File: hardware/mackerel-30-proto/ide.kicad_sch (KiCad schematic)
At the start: 0 parts

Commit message: Mostly fixed the SIMM-72 footprint
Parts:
- added C29, C30: C, Capacitor_THT:C_Disc_D4.3mm_W1.9mm_P5.00mm, symbol Device:C
- added C31: 1000uF, Capacitor_THT:CP_Radial_D10.0mm_P5.00mm, symbol Device:C_Polarized
- added C32: 470uF, Capacitor_THT:CP_Radial_D8.0mm_P3.50mm, symbol Device:C_Polarized_US
- added D4: LED, LED_THT:LED_D5.0mm, symbol Device:LED
- added J12: Screw_Terminal_01x04, TerminalBlock:TerminalBlock_bornier-4_P5.08mm, symbol Connector:Screw_Terminal_01x04
- added J13: Conn_02x20_Odd_Even, Connector_IDC:IDC-Header_2x20_P2.54mm_Vertical, symbol Connector_Generic:Conn_02x20_Odd_Even
- added R26, R27: 4k7, Resistor_THT:R_Axial_DIN0207_L6.3mm_D2.5mm_P7.62mm_Horizontal, symbol Device:R
- added R28: 470, Resistor_THT:R_Axial_DIN0207_L6.3mm_D2.5mm_P7.62mm_Horizontal, symbol Device:R
- added U12, U13: 74HC245, Package_DIP:DIP-20_W7.62mm_Socket, symbol 74xx:74HC245
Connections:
- new net: D4.2 (A), R28.2
- new net: D4.1 (K), J13.39 (Pin_39)
- new net +12V: C31.1, J12.1 (Pin_1)
- new net +5V: C29.1, C30.1, C32.1, J12.4 (Pin_4), R28.1, U12.20 (VCC), U13.20 (VCC)
- new net A1: J13.35 (Pin_35)
- new net A2: J13.33 (Pin_33)
- new net A3: J13.36 (Pin_36)
- new net D16: U13.18 (B0)
- new net D17: U13.17 (B1)
- new net D18: U13.16 (B2)
- new net D19: U13.15 (B3)
- new net D20: U13.14 (B4)
- new net D21: U13.13 (B5)
- new net D22: U13.12 (B6)
- new net D23: U13.11 (B7)
- new net D24: U12.18 (B0)
- new net D25: U12.17 (B1)
- new net D26: U12.16 (B2)
- new net D27: U12.15 (B3)
- new net D28: U12.14 (B4)
- new net D29: U12.13 (B5)
- new net D30: U12.12 (B6)
- new net D31: U12.11 (B7)
- new net GND: C29.2, C30.2, C31.2, C32.2, J12.2 (Pin_2), J12.3 (Pin_3), J13.19 (Pin_19), J13.2 (Pin_2), J13.22 (Pin_22), J13.24 (Pin_24), J13.26 (Pin_26), J13.30 (Pin_30), J13.40 (Pin_40), R26.1, R27.1, U12.10 (GND), U13.10 (GND)
- new net IDE_D0: J13.17 (Pin_17), U12.2 (A0)
- new net IDE_D1: J13.15 (Pin_15), U12.3 (A1)
- new net IDE_D10: J13.8 (Pin_8), U13.7 (A5)
- new net IDE_D11: J13.10 (Pin_10), U13.6 (A4)
- new net IDE_D12: J13.12 (Pin_12), U13.5 (A3)
- new net IDE_D13: J13.14 (Pin_14), U13.4 (A2)
- new net IDE_D14: J13.16 (Pin_16), U13.3 (A1)
- new net IDE_D15: J13.18 (Pin_18), U13.2 (A0)
- new net IDE_D2: J13.13 (Pin_13), U12.4 (A2)
- new net IDE_D3: J13.11 (Pin_11), U12.5 (A3)
- new net IDE_D4: J13.9 (Pin_9), U12.6 (A4)
- new net IDE_D5: J13.7 (Pin_7), U12.7 (A5)
- new net IDE_D6: J13.5 (Pin_5), U12.8 (A6)
- new net IDE_D7: J13.3 (Pin_3), U12.9 (A7)
- new net IDE_D8: J13.4 (Pin_4), U13.9 (A7)
- new net IDE_D9: J13.6 (Pin_6), U13.8 (A6)
- new net IDE_INT: J13.31 (Pin_31), R27.2
- new net IDE_RDY: J13.27 (Pin_27), R26.2
- new net R/W: U12.1 (A->B), U13.1 (A->B)
- new net /IDE_BUF: U12.19 (CE), U13.19 (CE)
- new net /IDE_CS0: J13.37 (Pin_37)
- new net /IDE_CS1: J13.38 (Pin_38)
- new net /IDE_RD: J13.25 (Pin_25)
- new net /IDE_WR: J13.23 (Pin_23)
- new net /RESET: J13.1 (Pin_1)
- no-connect marks 0 -> 6
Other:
- note added: "Activity LED"
- note added: "Basically DTACK, active HIGH"
- note added: "IDE Header"
- note added: "IRQ, active HIGH"
- note added: "NOTE: High and low bytes swapped between the CPU and the IDE header"

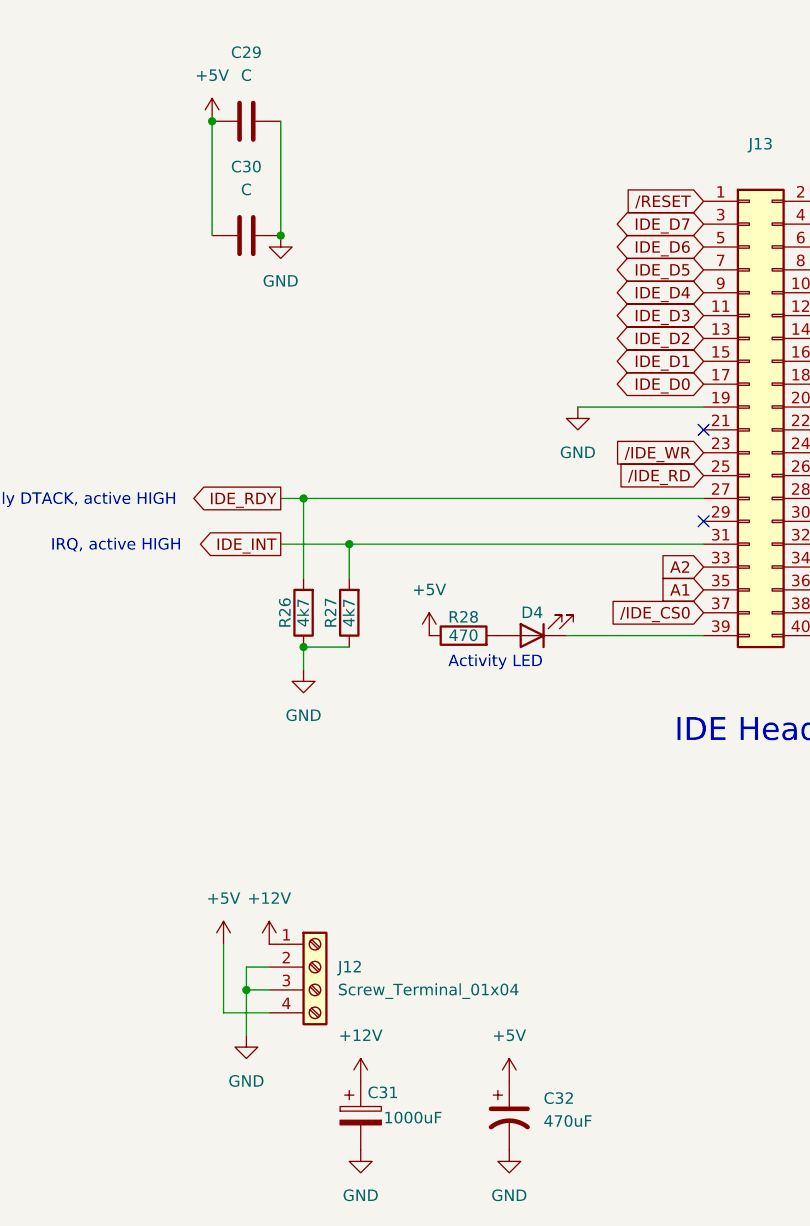
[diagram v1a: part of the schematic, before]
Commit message: Add DS1233 for reset
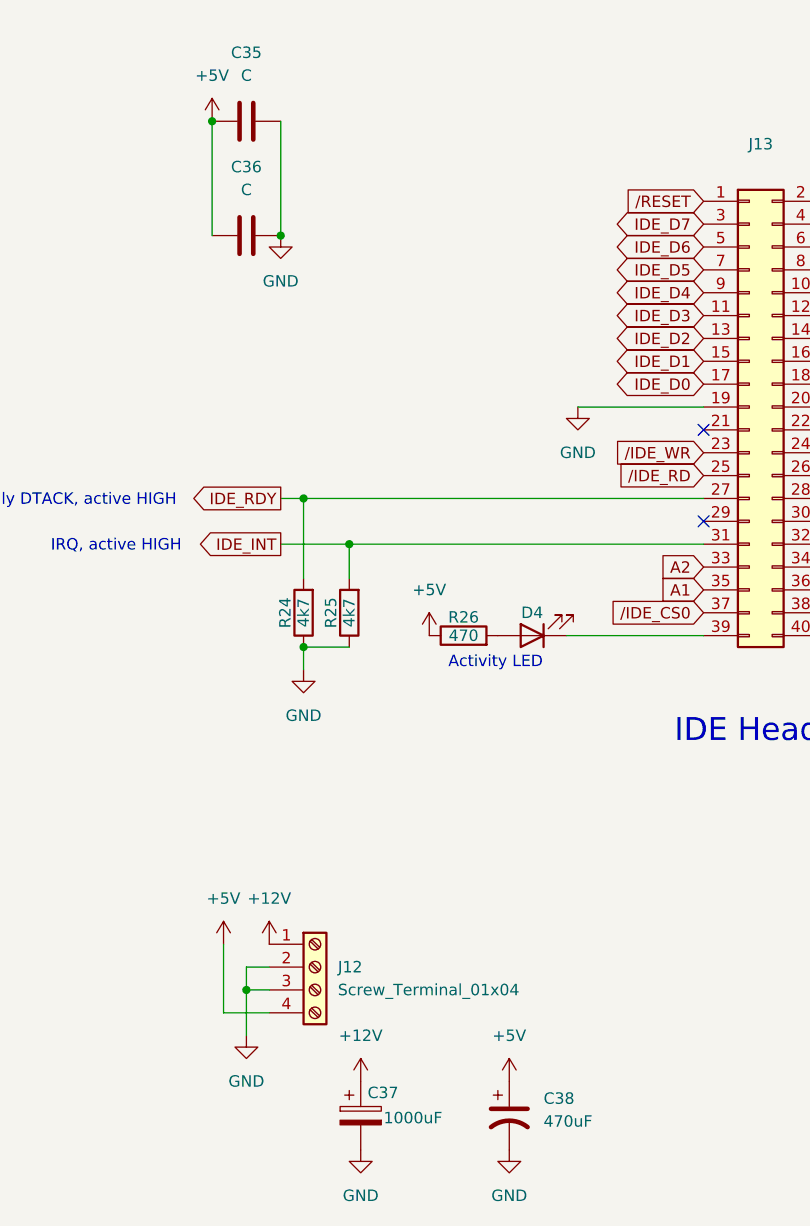
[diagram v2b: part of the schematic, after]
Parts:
- renumbered C29 to C35, C30 to C36, C31 to C37, C32 to C38, R26 to R24, R27 to R25, R28 to R26
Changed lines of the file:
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@@
 		(on_board yes)
 		(dnp no)
-		(property "Reference" "C31"
+		(property "Reference" "C37"
 			(at 159.512 148.59 0)
 			(effects
@@
 			(project "mackerel-30-proto"
 				(path "/9307474f-ec99-494d-b4c9-fbd0b10ce86a/b80ba0ac-a3c1-4262-b297-c092dfcb6fec"
-					(reference "C31")
+					(reference "C37")
 					(unit 1)
 				)
@@
 		(on_board yes)
 		(dnp no)
-		(property "Reference" "R28"
+		(property "Reference" "R26"
 			(at 170.18 95.758 90)
 			(effects
@@
 			(project "mackerel-30-proto"
 				(path "/9307474f-ec99-494d-b4c9-fbd0b10ce86a/b80ba0ac-a3c1-4262-b297-c092dfcb6fec"
-					(reference "R28")
+					(reference "R26")
 					(unit 1)
 				)
@@
 		(dnp no)
 		(fields_autoplaced yes)
-		(property "Reference" "C32"
+		(property "Reference" "C38"
 			(at 179.07 149.2249 0)
 			(effects
@@
 			(project "mackerel-30-proto"
 				(path "/9307474f-ec99-494d-b4c9-fbd0b10ce86a/b80ba0ac-a3c1-4262-b297-c092dfcb6fec"
-					(reference "C32")
+					(reference "C38")
 					(unit 1)
 				)
@@
 		(on_board yes)
 		(dnp no)
-		(property "Reference" "R26"
+		(property "Reference" "R24"
 			(at 150.368 95.25 90)
 			(effects
@@
 			(project "mackerel-30-proto"
 				(path "/9307474f-ec99-494d-b4c9-fbd0b10ce86a/b80ba0ac-a3c1-4262-b297-c092dfcb6fec"
-					(reference "R26")
+					(reference "R24")
 					(unit 1)
 				)
@@
 		(dnp no)
 		(fields_autoplaced yes)
-		(property "Reference" "C29"
+		(property "Reference" "C35"
 			(at 146.05 33.02 90)
 			(effects
@@
 			(project "mackerel-30-proto"
 				(path "/9307474f-ec99-494d-b4c9-fbd0b10ce86a/b80ba0ac-a3c1-4262-b297-c092dfcb6fec"
-					(reference "C29")
+					(reference "C35")
 					(unit 1)
 				)
@@
 		(dnp no)
 		(fields_autoplaced yes)
-		(property "Reference" "C30"
+		(property "Reference" "C36"
 			(at 146.05 45.72 90)
 			(effects
@@
 			(project "mackerel-30-proto"
 				(path "/9307474f-ec99-494d-b4c9-fbd0b10ce86a/b80ba0ac-a3c1-4262-b297-c092dfcb6fec"
-					(reference "C30")
+					(reference "C36")
 					(unit 1)
 				)
@@
 		(on_board yes)
 		(dnp no)
-		(property "Reference" "R27"
+		(property "Reference" "R25"
 			(at 155.448 95.25 90)
 			(effects
@@
 			(project "mackerel-30-proto"
 				(path "/9307474f-ec99-494d-b4c9-fbd0b10ce86a/b80ba0ac-a3c1-4262-b297-c092dfcb6fec"
-					(reference "R27")
-					(unit 1)
-				)
+					(reference "R25")
+					(unit 1)
+				)

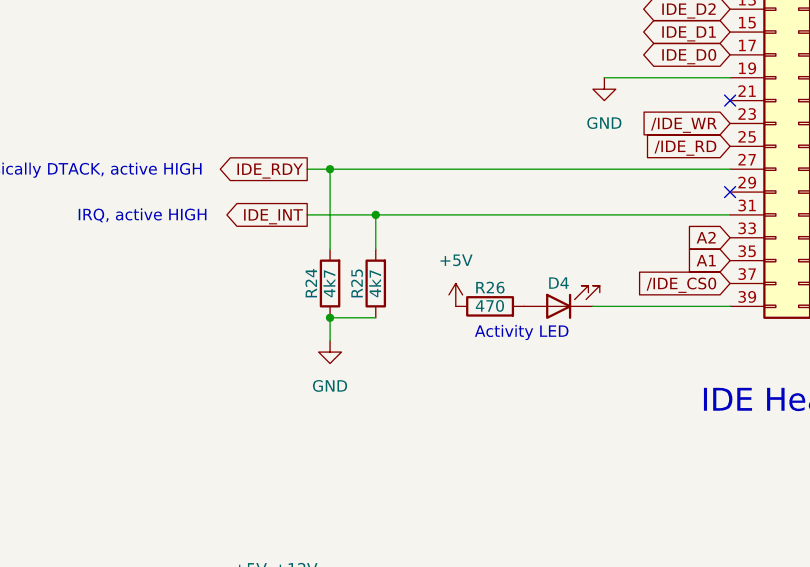
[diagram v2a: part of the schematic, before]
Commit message: rough layout of the PCB components
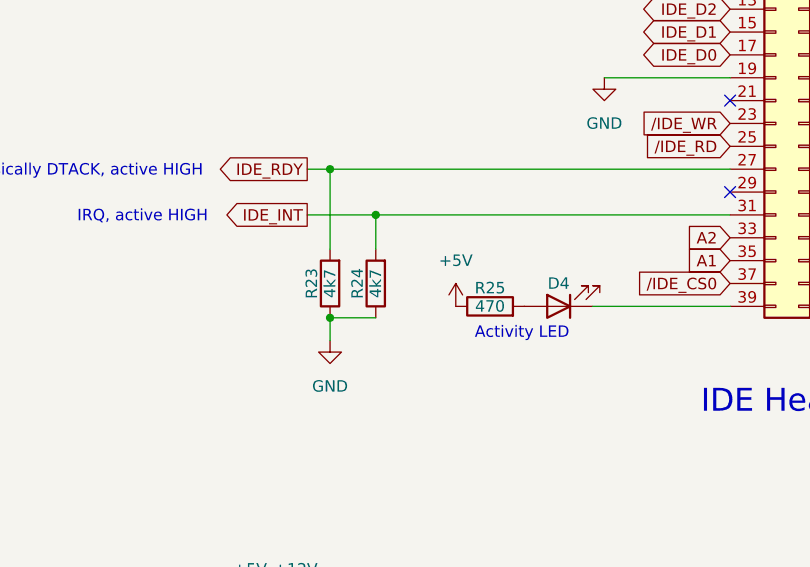
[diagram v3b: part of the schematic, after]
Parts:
- renumbered R24 to R23, R25 to R24, R26 to R25
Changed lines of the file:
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@@
 		(on_board yes)
 		(dnp no)
-		(property "Reference" "R26"
+		(property "Reference" "R25"
 			(at 170.18 95.758 90)
 			(effects
@@
 			(project "mackerel-30-proto"
 				(path "/9307474f-ec99-494d-b4c9-fbd0b10ce86a/b80ba0ac-a3c1-4262-b297-c092dfcb6fec"
-					(reference "R26")
+					(reference "R25")
 					(unit 1)
 				)
@@
 		(on_board yes)
 		(dnp no)
-		(property "Reference" "R24"
+		(property "Reference" "R23"
 			(at 150.368 95.25 90)
 			(effects
@@
 			(project "mackerel-30-proto"
 				(path "/9307474f-ec99-494d-b4c9-fbd0b10ce86a/b80ba0ac-a3c1-4262-b297-c092dfcb6fec"
-					(reference "R24")
+					(reference "R23")
 					(unit 1)
 				)
@@
 		(on_board yes)
 		(dnp no)
-		(property "Reference" "R25"
+		(property "Reference" "R24"
 			(at 155.448 95.25 90)
 			(effects
@@
 			(project "mackerel-30-proto"
 				(path "/9307474f-ec99-494d-b4c9-fbd0b10ce86a/b80ba0ac-a3c1-4262-b297-c092dfcb6fec"
-					(reference "R25")
-					(unit 1)
-				)
+					(reference "R24")
+					(unit 1)
+				)

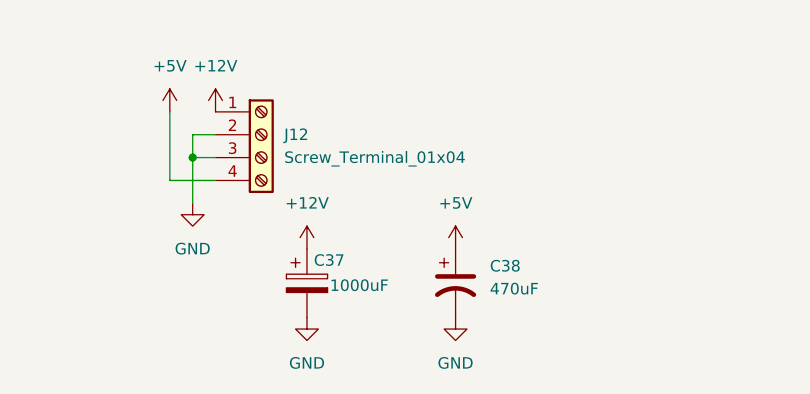
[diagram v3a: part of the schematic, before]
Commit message: Routed power supply section
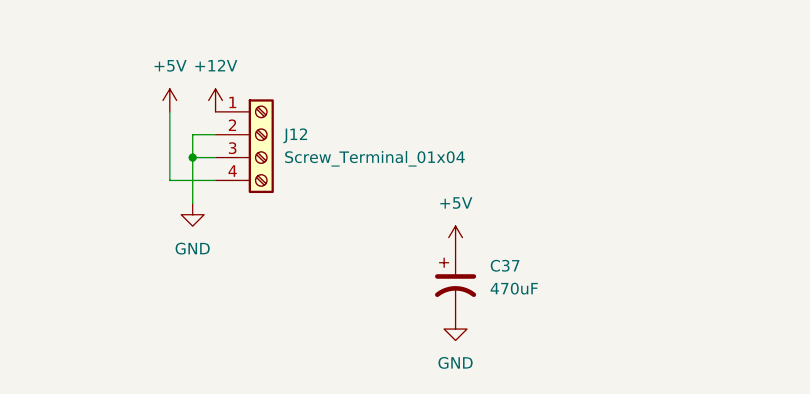
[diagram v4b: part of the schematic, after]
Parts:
- removed C37: 1000uF, Capacitor_THT:CP_Radial_D10.0mm_P5.00mm, symbol Device:C_Polarized
- renumbered C38 to C37
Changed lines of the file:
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@@
 		(dnp no)
 		(fields_autoplaced yes)
-		(property "Reference" "#PWR086"
+		(property "Reference" "#PWR084"
 			(at 175.26 151.13 0)
 			(effects
@@
 			(project "mackerel-30-proto"
 				(path "/9307474f-ec99-494d-b4c9-fbd0b10ce86a/b80ba0ac-a3c1-4262-b297-c092dfcb6fec"
-					(reference "#PWR086")
+					(reference "#PWR084")
 					(unit 1)
 				)
@@
 		(dnp no)
 		(fields_autoplaced yes)
-		(property "Reference" "#PWR089"
+		(property "Reference" "#PWR087"
 			(at 232.41 109.22 0)
 			(effects
@@
 			(project "mackerel-30-proto"
 				(path "/9307474f-ec99-494d-b4c9-fbd0b10ce86a/b80ba0ac-a3c1-4262-b297-c092dfcb6fec"
-					(reference "#PWR089")
-					(unit 1)
-				)
-			)
-		)
-	)
-	(symbol
-		(lib_id "power:GND")
-		(at 158.75 154.94 0)
-		(unit 1)
-		(exclude_from_sim no)
-		(in_bom yes)
-		(on_board yes)
-		(dnp no)
-		(fields_autoplaced yes)
-		(property "Reference" "#PWR084"
-			(at 158.75 161.29 0)
-			(effects
-				(font
-					(size 1.27 1.27)
-				)
-				(hide yes)
-			)
-		)
-		(property "Value" "GND"
-			(at 158.75 160.02 0)
-			(effects
-				(font
-					(size 1.27 1.27)
-				)
-			)
-		)
-		(property "Footprint" ""
-			(at 158.75 154.94 0)
-			(effects
-				(font
-					(size 1.27 1.27)
-				)
-				(hide yes)
-			)
-		)
-		(property "Datasheet" ""
-			(at 158.75 154.94 0)
-			(effects
-				(font
-					(size 1.27 1.27)
-				)
-				(hide yes)
-			)
-		)
-		(property "Description" "Power symbol creates a global label with name \"GND\" , ground"
-			(at 158.75 154.94 0)
-			(effects
-				(font
-					(size 1.27 1.27)
-				)
-				(hide yes)
-			)
-		)
-		(pin "1"
-		)
-		(instances
-			(project "mackerel-30-proto"
-				(path "/9307474f-ec99-494d-b4c9-fbd0b10ce86a/b80ba0ac-a3c1-4262-b297-c092dfcb6fec"
-					(reference "#PWR084")
-					(unit 1)
-				)
-			)
-		)
-	)
-	(symbol
-		(lib_id "Device:C_Polarized")
-		(at 158.75 151.13 0)
-		(unit 1)
-		(exclude_from_sim no)
-		(in_bom yes)
-		(on_board yes)
-		(dnp no)
-		(property "Reference" "C37"
-			(at 159.512 148.59 0)
-			(effects
-				(font
-					(size 1.27 1.27)
-				)
-				(justify left)
-			)
-		)
-		(property "Value" "1000uF"
-			(at 161.29 151.384 0)
-			(effects
-				(font
-					(size 1.27 1.27)
-				)
-				(justify left)
-			)
-		)
-		(property "Footprint" "Capacitor_THT:CP_Radial_D10.0mm_P5.00mm"
-			(at 159.7152 154.94 0)
-			(effects
-				(font
-					(size 1.27 1.27)
-				)
-				(hide yes)
-			)
-		)
-		(property "Datasheet" "~"
-			(at 158.75 151.13 0)
-			(effects
-				(font
-					(size 1.27 1.27)
-				)
-				(hide yes)
-			)
-		)
-		(property "Description" "Polarized capacitor"
-			(at 158.75 151.13 0)
-			(effects
-				(font
-					(size 1.27 1.27)
-				)
-				(hide yes)
-			)
-		)
-		(pin "1"
-		)
-		(pin "2"
-		)
-		(instances
-			(project "mackerel-30-proto"
-				(path "/9307474f-ec99-494d-b4c9-fbd0b10ce86a/b80ba0ac-a3c1-4262-b297-c092dfcb6fec"
-					(reference "C37")
+					(reference "#PWR087")
 					(unit 1)
 				)
@@
 	)
 	(symbol
-		(lib_id "power:+12V")
-		(at 158.75 147.32 0)
-		(unit 1)
-		(exclude_from_sim no)
-		(in_bom yes)
-		(on_board yes)
-		(dnp no)
-		(fields_autoplaced yes)
-		(property "Reference" "#PWR083"
-			(at 158.75 151.13 0)
-			(effects
-				(font
-					(size 1.27 1.27)
-				)
-				(hide yes)
-			)
-		)
-		(property "Value" "+12V"
-			(at 158.75 142.24 0)
-			(effects
-				(font
-					(size 1.27 1.27)
-				)
-			)
-		)
-		(property "Footprint" ""
-			(at 158.75 147.32 0)
-			(effects
-				(font
-					(size 1.27 1.27)
-				)
-				(hide yes)
-			)
-		)
-		(property "Datasheet" ""
-			(at 158.75 147.32 0)
-			(effects
-				(font
-					(size 1.27 1.27)
-				)
-				(hide yes)
-			)
-		)
-		(property "Description" "Power symbol creates a global label with name \"+12V\""
-			(at 158.75 147.32 0)
-			(effects
-				(font
-					(size 1.27 1.27)
-				)
-				(hide yes)
-			)
-		)
-		(pin "1"
-		)
-		(instances
-			(project "mackerel-30-proto"
-				(path "/9307474f-ec99-494d-b4c9-fbd0b10ce86a/b80ba0ac-a3c1-4262-b297-c092dfcb6fec"
-					(reference "#PWR083")
-					(unit 1)
-				)
-			)
-		)
-	)
-	(symbol
 		(lib_id "Device:R")
 		(at 170.18 97.79 90)
@@
 		(dnp no)
 		(fields_autoplaced yes)
-		(property "Reference" "C38"
+		(property "Reference" "C37"
 			(at 179.07 149.2249 0)
 			(effects
@@
 			(project "mackerel-30-proto"
 				(path "/9307474f-ec99-494d-b4c9-fbd0b10ce86a/b80ba0ac-a3c1-4262-b297-c092dfcb6fec"
-					(reference "C38")
+					(reference "C37")
 					(unit 1)
 				)
@@
 		(dnp no)
 		(fields_autoplaced yes)
-		(property "Reference" "#PWR088"
+		(property "Reference" "#PWR086"
 			(at 182.88 78.74 0)
 			(effects
@@
 			(project "mackerel-30-proto"
 				(path "/9307474f-ec99-494d-b4c9-fbd0b10ce86a/b80ba0ac-a3c1-4262-b297-c092dfcb6fec"
-					(reference "#PWR088")
+					(reference "#PWR086")
 					(unit 1)
 				)
@@
 		(dnp no)
 		(fields_autoplaced yes)
-		(property "Reference" "#PWR085"
+		(property "Reference" "#PWR083"
 			(at 166.37 101.6 0)
 			(effects
@@
 			(project "mackerel-30-proto"
 				(path "/9307474f-ec99-494d-b4c9-fbd0b10ce86a/b80ba0ac-a3c1-4262-b297-c092dfcb6fec"
-					(reference "#PWR085")
+					(reference "#PWR083")
 					(unit 1)
 				)
@@
 		(dnp no)
 		(fields_autoplaced yes)
-		(property "Reference" "#PWR087"
+		(property "Reference" "#PWR085"
 			(at 175.26 161.29 0)
 			(effects
@@
 			(project "mackerel-30-proto"
 				(path "/9307474f-ec99-494d-b4c9-fbd0b10ce86a/b80ba0ac-a3c1-4262-b297-c092dfcb6fec"
-					(reference "#PWR087")
-					(unit 1)
-				)
+					(reference "#PWR085")
+					(unit 1)
+				)
